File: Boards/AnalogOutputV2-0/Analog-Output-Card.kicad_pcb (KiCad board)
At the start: 2 copper layers, 72 x 72 mm, 60 parts, among them IC1 PIC16F1936, J1 5Vdc Jumper, P1 AquaPicBus, P2 ICSP, P3 Power, P4 Dimming Outputs, Q1 AO3407A, Q2 AO3407A, U1 LM358, U2 LM358, U3 ST485EC, U4 TS5A4624, U5 TS5A4624, U6 TS5A4624, U7 TS5A4624, X1 8MHz

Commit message: working on Analog Output card
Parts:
- removed ?: , Symbols:Symbol_OSHW-Logo_SilkScreen
- removed J1: 5Vdc Jumper, Pin_Headers:Pin_Header_Straight_1x03
- removed LOGO: Val**, A_MyFootPrints:AquaPic_Logo
- added C*: 4u7, Capacitors_SMD:C_0805, F.Cu at (4.45, -51.4)
- added C*: 4u7, Capacitors_SMD:C_0805, F.Cu at (6.99, -51.4)
- added C*: 100nF, Capacitors_SMD:C_0805, F.Cu at (19.1, -24.1)
- added C19: 4u7, Capacitors_SMD:C_0805, F.Cu at (204.1, -22.3)
- added C20: 100nF, Capacitors_SMD:C_0805, F.Cu at (193.6, -11.6)
- added D*: APT2012, LEDs:LED-0805, F.Cu at (73.7, -59.7)
- added D*: SMTL4-RGY, MyFootPrints:PLCC-4, F.Cu at (73.7, -67.3)
- added G***: LOGO, MyFootPrints:AquaPic_Logo_Small, F.Cu at (6.99, -32.4)
- added ICSP: 5x1 2.54, Pin_Headers:Pin_Header_Straight_1x06_Pitch2.54mm, F.Cu at (33.7, -67.3)
- added Q*: NX7002AK, TO_SOT_Packages_SMD:SOT-23, F.Cu at (18.4, -49.5)
- added Q*: NX7002AK, TO_SOT_Packages_SMD:SOT-23, F.Cu at (18.4, -43.8)
- added Q*: NX7002AK, TO_SOT_Packages_SMD:SOT-23, F.Cu at (18.4, -37.5)
- added Q3: NX7002AK, TO_SOT_Packages_SMD:SOT-23, F.Cu at (158.2, -6.89)
- added Q4: NX7002AK, TO_SOT_Packages_SMD:SOT-23, F.Cu at (173.3, -21.3)
- added Q5: NX7002AK, TO_SOT_Packages_SMD:SOT-23, F.Cu at (143.9, 11.0)
- added Q6: NX7002AK, TO_SOT_Packages_SMD:SOT-23, F.Cu at (135.6, 14.7)
- added Q7: NX7002AK, TO_SOT_Packages_SMD:SOT-23, F.Cu at (151.9, 0.16)
- added Q8: NX7002AK, TO_SOT_Packages_SMD:SOT-23, F.Cu at (143.9, 4.06)
- added Q9: NX7002AK, TO_SOT_Packages_SMD:SOT-23, F.Cu at (164.2, -15.9)
- added R*: 150R, Resistors_SMD:R_0805, F.Cu at (64.8, -64.8)
- added R*: 150R, Resistors_SMD:R_0805, F.Cu at (64.8, -59.7)
- added R*: 4K99, Resistors_SMD:R_0805, F.Cu at (14.0, -38.6)
- added R*: 150R, Resistors_SMD:R_0805, F.Cu at (64.8, -62.2)
- added R*: 150R, Resistors_SMD:R_0805, F.Cu at (64.8, -67.3)
- added R*: 1K, Resistors_SMD:R_0805, F.Cu at (14.0, -53.3)
- added R*: 10K, Resistors_SMD:R_0805, F.Cu at (14.0, -50.8)
- added R*: 10K, Resistors_SMD:R_0805, F.Cu at (14.0, -48.3)
- added R*: 4K99, Resistors_SMD:R_0805, F.Cu at (14.0, -45.1)
- added R*: 4K99, Resistors_SMD:R_0805, F.Cu at (14.0, -42.5)
- added R*: 4K99, Resistors_SMD:R_0805, F.Cu at (14.0, -36.2)
- added R22: 4K99, Resistors_SMD:R_0805, F.Cu at (178.2, -4.44)
- added R23: 4K99, Resistors_SMD:R_0805, F.Cu at (189.0, -11.5)
- added R24: 1K, Resistors_SMD:R_0805, F.Cu at (182.0, -4.44)
- added R25: 10K, Resistors_SMD:R_0805, F.Cu at (168.3, 9.56)
- added R26: 4K99, Resistors_SMD:R_0805, F.Cu at (161.0, 11.5)
- added R27: 4K99, Resistors_SMD:R_0805, F.Cu at (137.3, 20.8)
- added R28: 10K, Resistors_SMD:R_0805, F.Cu at (185.2, -22.2)
- added R29: 4K99, Resistors_SMD:R_0805, F.Cu at (170.6, -8.19)
- added R30: 4K99, Resistors_SMD:R_0805, F.Cu at (157.9, 6.16)
- added R31: 4K99, Resistors_SMD:R_0805, F.Cu at (164.8, -1.14)
- added R32: 4K99, Resistors_SMD:R_0805, F.Cu at (150.0, 13.3)
- added R33: 4K99, Resistors_SMD:R_0805, F.Cu at (161.7, 16.9)
- added R34: 4K99, Resistors_SMD:R_0805, F.Cu at (168.3, 4.21)
- added R35: 4K99, Resistors_SMD:R_0805, F.Cu at (200.1, -22.2)
- added R36: 4K99, Resistors_SMD:R_0805, F.Cu at (178.2, 0.91)
- added REF***: OSHW-Logo2_14.6x12mm_SilkScreen, Symbols:OSHW-Logo2_14.6x12mm_SilkScreen, B.Cu at (54.0, -25.4)
- added U*: AP2114H, TO_SOT_Packages_SMD:SOT-223, F.Cu at (6.99, -44.5)
- added U8: AP2114H, TO_SOT_Packages_SMD:SOT-223, F.Cu at (114.3, -6.99)
- C10: value 100nF -> 4u7
- C4: value 470pF -> 100nF
- D1: value SMP4-RGY -> SMTL4-RGY; footprint A_MyFootPrints:PLCC-4 -> MyFootPrints:PLCC-4
- D2, D3: footprint LEDs:LED-0805 -> LEDs:LED_0805
- IC1: value PIC16F1936 -> PIC32MM0064GPM028; footprint Housings_SOIC:SOIC-28_7.5x17.9mm_Pitch1.27mm -> Housings_SSOP:SSOP-28_5.3x10.2mm_Pitch0.65mm
- P1: value AquaPicBus -> 8x1 2.54; footprint A_MyFootPrints:USB-1.1_Stacked -> MyFootPrints:Screw_Header_1x8
- P2: value ICSP -> Stacked USBA; footprint Pin_Headers:Pin_Header_Straight_1x06 -> MyFootPrints:USB-1.1_Stacked
- P3: value Power -> 4x1 2.54; footprint A_MyFootPrints:Screw_Header_1x4 -> MyFootPrints:Screw_Header_1x4
- P4: value Dimming Outputs -> 6x1 2.54 Pin Header; footprint A_MyFootPrints:Screw_Header_1x8 -> Pin_Headers:Pin_Header_Straight_1x06_Pitch2.54mm
- Q1, Q2: footprint Housings_SOT-23_SOT-143_TSOT-6:SOT-23 -> TO_SOT_Packages_SMD:SOT-23
- R17, R18, R19, R20: value 300R -> 150R
- U4, U5, U6, U7: value TS5A4624 -> DG469; footprint A_MyFootPrints:TSSOP-6_SC-70-6 -> Housings_SSOP:TSSOP-8_3x3mm_Pitch0.65mm
- X1: footprint A_MyFootPrints:Resonator_3.2x1.3 -> MyFootPrints:Resonator_3.2x1.3
- moved C4 182.1 mm to (203.4, -11.9), turned to 0 degrees
- moved C10 181.4 mm to (193.8, -6.44), turned to 0 degrees
- moved R5 172.7 mm to (193.6, -16.8), turned to 0 degrees
- moved C5 169.9 mm to (192.5, -1.09), turned to 0 degrees
- moved C15 165.1 mm to (189.4, -6.29), turned to 0 degrees
- moved C7 164.0 mm to (187.6, -1.09), turned to 0 degrees
- moved C6 162.1 mm to (198.2, -6.44), turned to 0 degrees
- moved R3 154.4 mm to (188.7, -22.2), turned to 0 degrees
- moved C13 154.0 mm to (204.6, -17.1), turned to 0 degrees
- moved R6 153.7 mm to (172.1, 5.86), turned to 0 degrees
- moved C9 152.7 mm to (182.7, 5.96)
- moved R4 149.0 mm to (182.9, -15.1), turned to 0 degrees
- moved C11 148.1 mm to (198.2, -17.0), turned to 0 degrees
- moved C2 147.0 mm to (177.4, 11.3), turned to 0 degrees
- moved C16 145.7 mm to (177.4, 6.11), turned to 0 degrees
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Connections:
- net /12Vdc renamed Net-(P3-Pad3)
- net /5Vdc renamed Net-(P3-Pad1)
- C1 pad 1: +5V -> +3V3
- C13 pad 2: /D_OUT3 -> /A3
- C14 pad 2: /D_OUT4 -> /A4
- C15 pad 1: +5V -> +12V
- C16 pad 1: +5V -> +12V
- C17 pad 1: +5V -> +12V
- C18 pad 1: +5V -> +12V
- C2 pad 1: +5V -> +3V3
- C7 pad 2: /D_OUT1 -> /A1
- C8 pad 2: /D_OUT2 -> /A2
- D1 pad 4: +5V -> +3V3
- D2 pad 1: Net-(D2-Pad1) -> GND
- D2 pad 2: GND -> Net-(D2-Pad2)
- D3 pad 1: Net-(D3-Pad1) -> GND
- D3 pad 2: GND -> Net-(D3-Pad2)
- IC1 pad 12: /PWM2 -> /RELAY1
- IC1 pad 13: /PWM1 -> +3V3
- IC1 pad 14: Net-(IC1-Pad14) -> /RELAY2
- IC1 pad 15: Net-(IC1-Pad15) -> /RELAY3
- IC1 pad 16: /T_nR -> /RELAY4
- IC1 pad 17: /TX -> //RTS
- IC1 pad 18: /RX -> //RTS
- IC1 pad 19: GND -> Net-(IC1-Pad19)
- IC1 pad 2: /STAT_LED_R -> /PGC
- IC1 pad 20: +5V -> Net-(C4-Pad1)
- IC1 pad 21: /PWM4 -> /LED_Y
- IC1 pad 22: /RELAY1 -> /LED_G
- IC1 pad 23: /RELAY2 -> GND
- IC1 pad 24: /RELAY3 -> /LED_R
- IC1 pad 25: /RELAY4 -> /TX_LV
- IC1 pad 26: /PWM3 -> /RX_LV
- IC1 pad 27: /PGC -> GND
- IC1 pad 28: /PGD -> +3V3
- IC1 pad 3: /STAT_LED_G -> /PGD
- IC1 pad 4: /STAT_LED_Y -> /PWM1_LV
- IC1 pad 5: Net-(IC1-Pad5) -> /PWM2_LV
- IC1 pad 6: Net-(IC1-Pad6) -> /PWM3_LV
- IC1 pad 7: Net-(C4-Pad1) -> /PWM4_LV
- P1 pad 1: /5VdcB -> /OUT1
- P1 pad 2: /D+ -> GND
- P1 pad 3: /D- -> /OUT2
- P1 pad 5: /5VdcB -> /OUT3
- P1 pad 6: /D+ -> GND
- P1 pad 7: /D- -> /OUT4
- P2 pad 1: //MCLR -> +5V
- P2 pad 2: +5V -> /A
- P2 pad 3: GND -> /B
- P2 pad 4: /PGD -> GND
- P2 pad 5: /PGC -> +5V
- P2 pad 6: Net-(P2-Pad6) -> /A
- P4 pad 1: /D_OUT1 -> //MCLR
- P4 pad 2: GND -> +3V3
- P4 pad 3: /D_OUT2 -> GND
- P4 pad 4: GND -> /PGD
- P4 pad 5: /D_OUT3 -> /PGC
- P4 pad 6: GND -> Net-(P4-Pad6)
- Q1 pad 2: /5VdcA -> +5V
- R1 pad 2: /D_OUT1 -> /A1
- R11 pad 2: /D_OUT4 -> /A4
- R13 pad 1: /A_OUT3 -> /PWM3
- R15 pad 1: /A_OUT4 -> /PWM4
- R17 pad 2: /STAT_LED_G -> /LED_G
- R18 pad 2: /STAT_LED_Y -> /LED_Y
- R19 pad 2: /STAT_LED_R -> /LED_R
- R20 pad 1: +5V -> +3V3
- R20 pad 2: Net-(D2-Pad1) -> Net-(D2-Pad2)
- R21 pad 2: Net-(D3-Pad1) -> Net-(D3-Pad2)
- R3 pad 2: /D_OUT2 -> /A2
- R5 pad 1: /A_OUT1 -> /PWM1
- R7 pad 1: /A_OUT2 -> /PWM2
- R9 pad 2: /D_OUT3 -> /A3
- U1 pad 1: /D_OUT1 -> /A1
- U1 pad 2: Net-(R1-Pad1) -> Net-(C5-Pad1)
- U1 pad 3: Net-(C5-Pad1) -> Net-(R1-Pad1)
- U1 pad 5: Net-(C6-Pad1) -> Net-(R3-Pad1)
- U1 pad 6: Net-(R3-Pad1) -> Net-(C6-Pad1)
- U1 pad 7: /D_OUT2 -> /A2
- U2 pad 1: /D_OUT3 -> /A3
- U2 pad 2: Net-(R10-Pad1) -> Net-(C11-Pad1)
- U2 pad 3: Net-(C11-Pad1) -> Net-(R10-Pad1)
- U2 pad 5: Net-(C12-Pad1) -> Net-(R11-Pad1)
- U2 pad 6: Net-(R11-Pad1) -> Net-(C12-Pad1)
- U2 pad 7: /D_OUT4 -> /A4
- U3 pad 2: /T_nR -> /RTS
- U3 pad 3: /T_nR -> /RTS
- U3 pad 6: /D+ -> /A
- U3 pad 7: /D- -> /B
- U4 pad 1: /RELAY1 -> /OUT1
- U4 pad 2: +5V -> /A1
- U4 pad 4: /A_OUT1 -> +12V
- U4 pad 5: /PWM1 -> Net-(U4-Pad5)
- U4 pad 6: /D_OUT1 -> /RELAY1
- U5 pad 1: /RELAY3 -> /OUT3
- U5 pad 2: +5V -> /A3
- U5 pad 4: /A_OUT3 -> +12V
- U5 pad 5: /PWM3 -> Net-(U5-Pad5)
- U5 pad 6: /D_OUT3 -> /RELAY3
- U6 pad 1: /RELAY2 -> /OUT2
- U6 pad 2: +5V -> /A2
- U6 pad 4: /A_OUT2 -> +12V
- U6 pad 5: /PWM2 -> Net-(U6-Pad5)
- U6 pad 6: /D_OUT2 -> /RELAY2
- U7 pad 1: /RELAY4 -> /OUT4
- U7 pad 2: +5V -> /A4
- U7 pad 4: /A_OUT4 -> +12V
- U7 pad 5: /PWM4 -> Net-(U7-Pad5)
- U7 pad 6: /D_OUT4 -> /RELAY4
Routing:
- net +5V: track 238.4 -> 5.75 mm, vias 5 -> 0
- net +12V: track 166.6 -> 0.00 mm, vias 5 -> 0
- net GND: track 72.1 -> 3.12 mm, vias 26 -> 4
- net /D_OUT3: track 66.1 -> 0.00 mm
- net /D_OUT4: track 58.7 -> 0.00 mm
- net /D_OUT1: track 51.0 -> 0.00 mm
- net /D_OUT2: track 49.6 -> 0.00 mm
- net /RELAY4: track 41.5 -> 0.00 mm, vias 2 -> 0
- net /D+: track 34.5 -> 0.00 mm
- net /D-: track 32.3 -> 0.00 mm
- net /RELAY3: track 32.0 -> 0.00 mm, vias 2 -> 0
- net /RELAY1: track 31.9 -> 0.00 mm, vias 4 -> 0
- net /5VdcB: track 30.0 -> 0.00 mm
- net /PWM3: track 29.9 -> 0.00 mm, vias 2 -> 0
- net /STAT_LED_R: track 28.2 -> 0.00 mm, vias 2 -> 0
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- removed copper zone on B.Cu, net GND
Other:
- board size 72 x 72 mm -> 80 x 72 mm
- copper layers 2 -> 4
- net class Default: via_dia 0.889 -> 0.6; via_drill 0.635 -> 0.4
- rule trace_min: 0.254 -> 0.2
- rule via_min_drill: 0.508 -> 0.3
- rule via_min_size: 0.889 -> 0.4
- board text added: "AquaPic Analog Output Card Rev 2 Goodtime Development Skyler Brandt"
- board text added: "Power Ok"
- board text removed: "12V"
- board text removed: "12V Power Ok"
- board text removed: "5V"
- board text removed: "5V Power Ok"
- board text removed: "AquaPic Dimming Rev 1.1 Skyler Brandt"
- board text removed: "Ch. 1"
- board text removed: "Ch. 2"
- board text removed: "Ch. 3"
- board text removed: "Ch. 4"

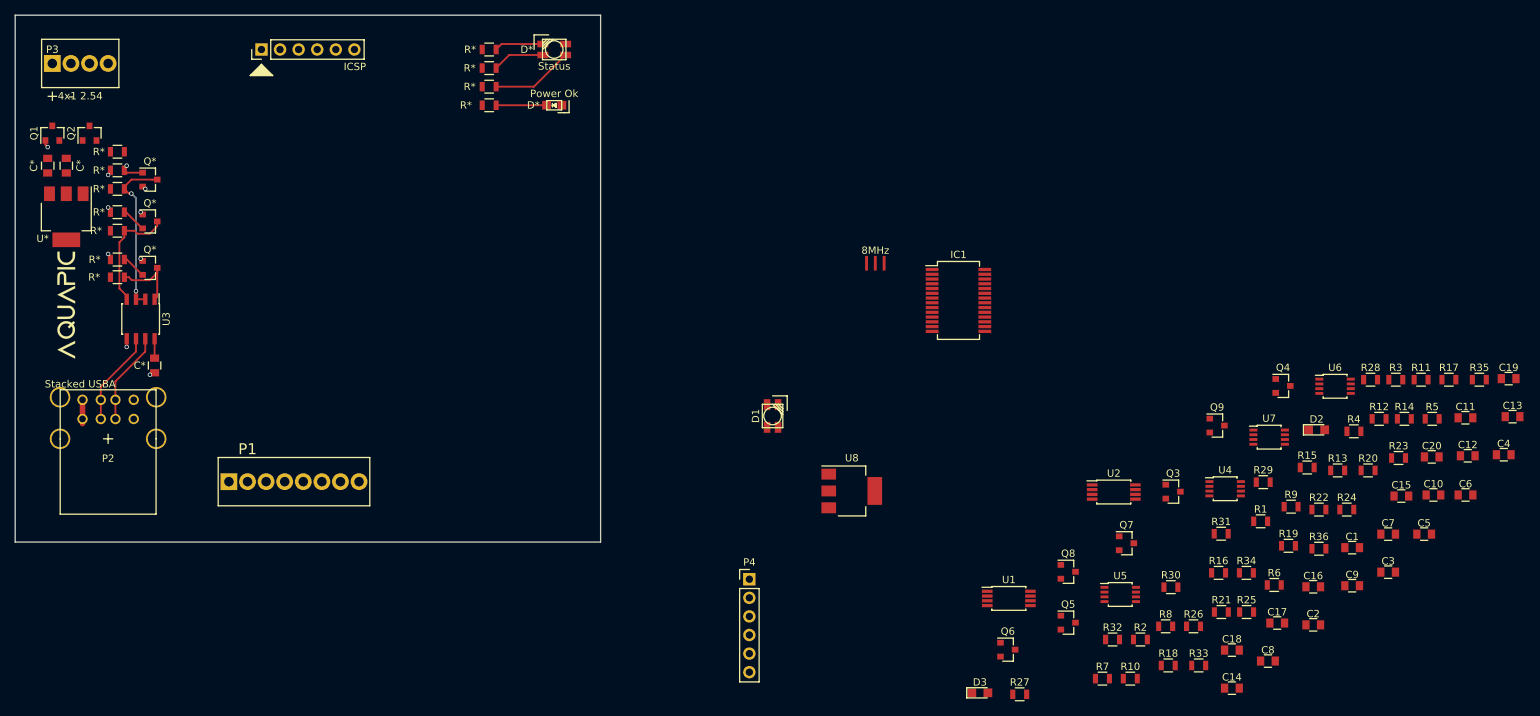
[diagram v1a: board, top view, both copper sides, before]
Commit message: worked on Analog Output Cardboard layout finished
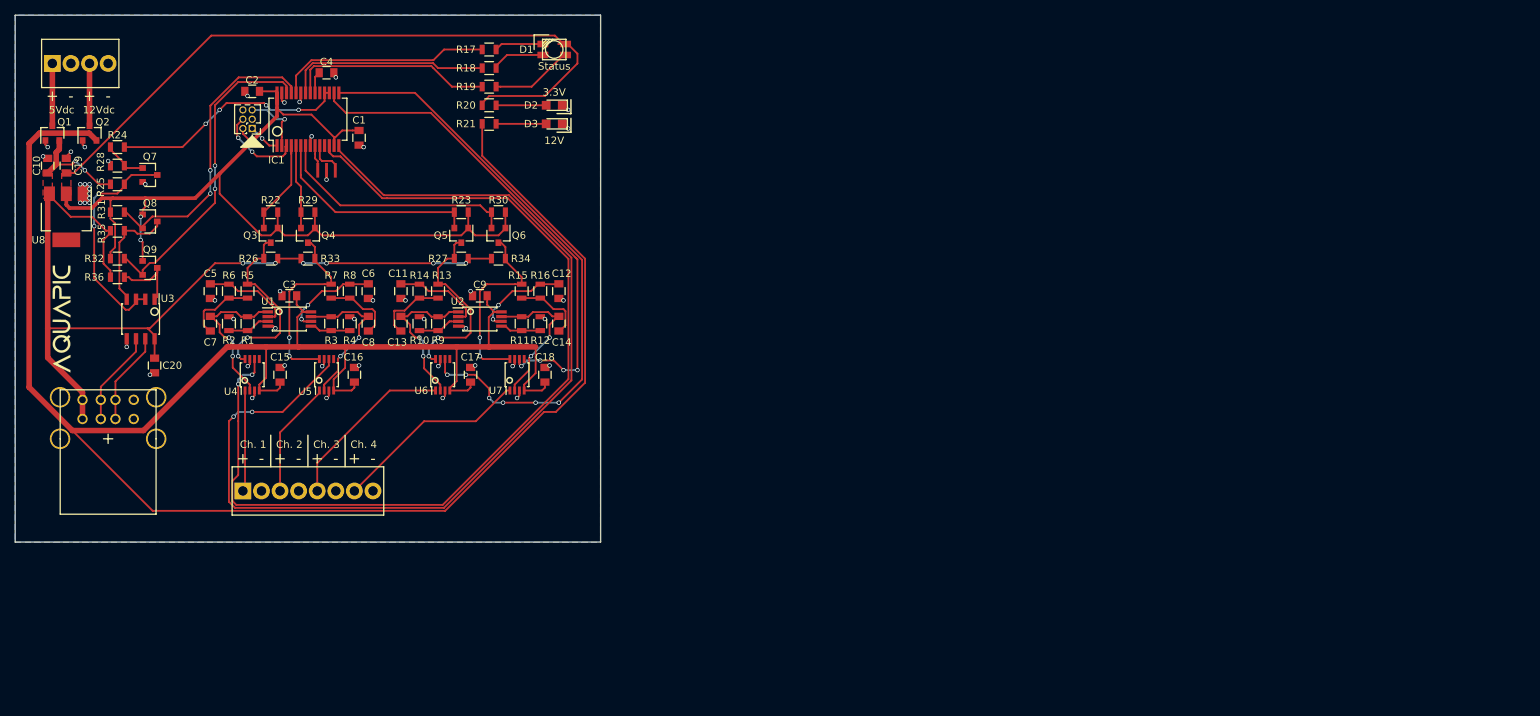
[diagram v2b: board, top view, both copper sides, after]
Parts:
- removed C* (x2): 4u7, Capacitors_SMD:C_0805
- removed C*: 100nF, Capacitors_SMD:C_0805
- removed D*: APT2012, LEDs:LED-0805
- removed D*: SMTL4-RGY, MyFootPrints:PLCC-4
- removed ICSP: 5x1 2.54, Pin_Headers:Pin_Header_Straight_1x06_Pitch2.54mm
- removed Q* (x3): NX7002AK, TO_SOT_Packages_SMD:SOT-23
- removed R* (x4): 150R, Resistors_SMD:R_0805
- removed R* (x4): 4K99, Resistors_SMD:R_0805
- removed R*: 1K, Resistors_SMD:R_0805
- removed R* (x2): 10K, Resistors_SMD:R_0805
- removed U*: AP2114H, TO_SOT_Packages_SMD:SOT-223
- P4: footprint Pin_Headers:Pin_Header_Straight_1x06_Pitch2.54mm -> Pin_Headers:Pin_Header_Straight_2x03_Pitch1.27mm
- moved C19 199.2 mm to (6.99, -51.4), turned to 90 degrees
- moved C10 194.6 mm to (4.45, -51.4), turned to 90 degrees
- moved R35 187.2 mm to (14.0, -42.5)
- moved R24 175.1 mm to (14.0, -54.0)
- moved C20 175.0 mm to (19.1, -24.1), turned to 270 degrees
- moved R28 173.3 mm to (14.0, -48.9)
- moved C5 169.2 mm to (26.7, -34.3), turned to 270 degrees
- moved C4 169.1 mm to (42.5, -64.1)
- moved R36 168.3 mm to (14.0, -36.2)
- moved R25 165.9 mm to (14.0, -51.4), turned to 180 degrees
- moved C7 163.5 mm to (26.7, -29.8), turned to 90 degrees
- moved R5 162.8 mm to (31.8, -34.3), turned to 270 degrees
- moved C2 162.3 mm to (32.4, -61.6), turned to 180 degrees
- moved R31 157.1 mm to (14.0, -45.1)
- moved C3 154.8 mm to (37.5, -33.7), turned to 180 degrees
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- renumbered Q6 to Q4, Q4 to Q5, Q7 to Q6, Q5 to Q7, R19 to R17, R17 to R18, R18 to R19, U6 to U5, U5 to U6
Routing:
- net +12V: track 0.00 -> 303.8 mm
- net +3V3: track 3.00 -> 231.6 mm, vias 4 -> 2
- net /RELAY2: track 0.00 -> 138.3 mm, vias 0 -> 2
- net /RELAY1: track 0.00 -> 130.7 mm, vias 0 -> 2
- net +5V: track 5.75 -> 134.8 mm, vias 0 -> 8
- net /RELAY3: track 0.00 -> 83.4 mm, vias 0 -> 6
- net /RELAY4: track 0.00 -> 68.1 mm, vias 0 -> 4
- net GND: track 3.12 -> 51.5 mm, vias 4 -> 50
- net /RX_LV: track 3.36 -> 43.3 mm, vias 0 -> 2
- net /TX_LV: track 3.41 -> 41.0 mm, vias 0 -> 2
- net /PWM4_LV: track 0.00 -> 33.4 mm
- net //RTS: track 0.00 -> 32.5 mm, vias 0 -> 4
- net /PWM3_LV: track 0.00 -> 29.5 mm
- net /LED_R: track 0.00 -> 29.3 mm
- net /LED_Y: track 0.00 -> 28.0 mm
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- added copper zone on F.Cu, net +3V3
- added copper zone on F.Cu, net +5V
- added copper zone on B.Cu, net GND
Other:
- copper layers 4 -> 2
- net class Default: via_dia 0.6 -> 0.5969; via_drill 0.4 -> 0.4064
- rule trace_min: 0.2 -> 0.2032
- rule via_min_size: 0.4 -> 0.4064
- board text added: "12V"
- board text added: "12Vdc"
- board text added: "3.3V"
- board text added: "5Vdc"
- board text added: "Ch. 1"
- board text added: "Ch. 2"
- board text added: "Ch. 3"
- board text added: "Ch. 4"
- board text removed: "Power Ok"

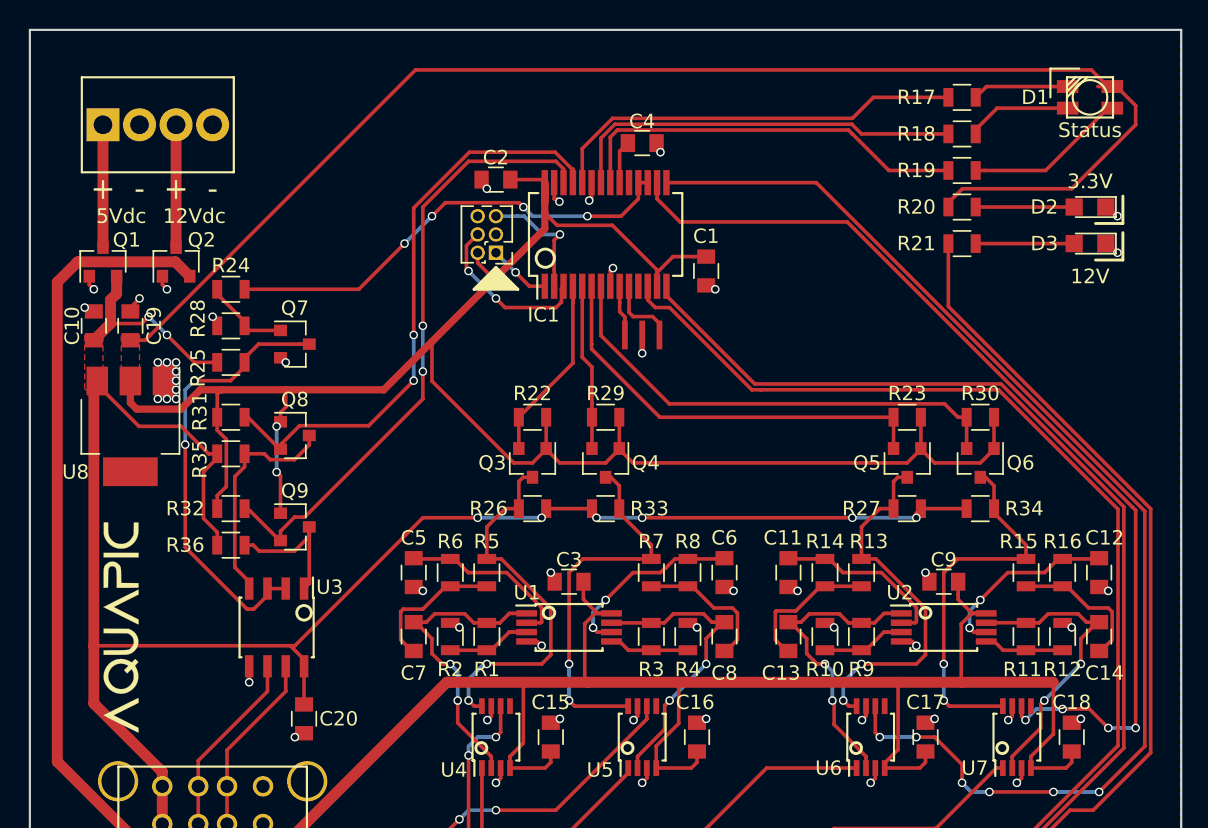
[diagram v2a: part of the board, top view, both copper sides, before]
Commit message: fixed placement on boards so everything is mostly in the same spot
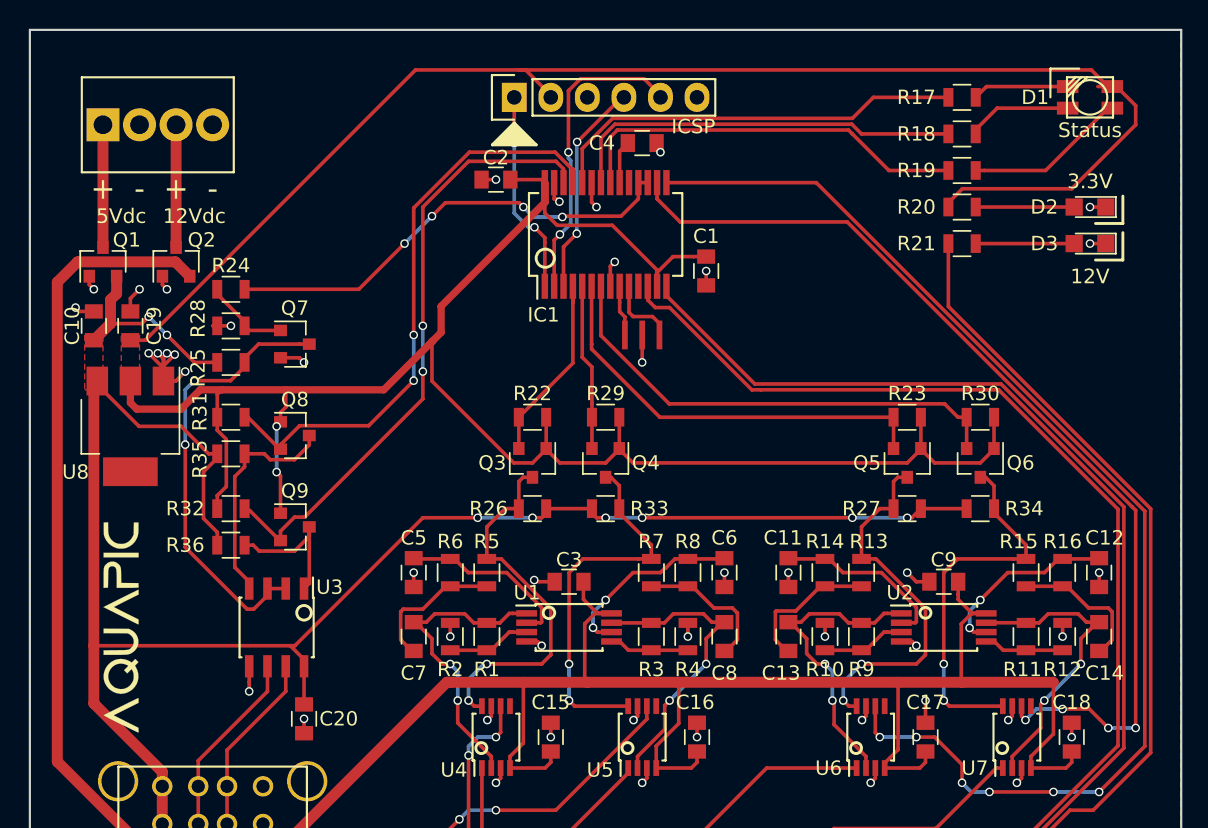
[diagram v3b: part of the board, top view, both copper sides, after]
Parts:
- ICSP: renamed from P4; footprint Pin_Headers:Pin_Header_Straight_2x03_Pitch1.27mm -> Pin_Headers:Pin_Header_Straight_1x06
- moved ICSP 10.9 mm to (33.7, -67.3), turned to 90 degrees
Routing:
- net GND: track 51.5 -> 68.0 mm, vias 50 -> 46
- net /PGC: track 8.74 -> 21.5 mm, vias 1 -> 2
- net //MCLR: track 4.36 -> 14.3 mm, vias 1 -> 2
- net /PGD: track 11.7 -> 15.0 mm
- net +3V3: track 231.6 -> 234.5 mm
